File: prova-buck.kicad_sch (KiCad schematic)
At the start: 36 parts, among them J1 Screw_Terminal_01x02, J2 Barrel_Jack, J3 USB_B_Micro, J4 Conn_02x03_Counter_Clockwise, J5 Conn_02x03_Counter_Clockwise, Q1 AO3401A, SW1 SW_SPDT, SW2 SW_SPDT, SW3 SW_SPDT, U1 MPQ9842GL, U2 LDL1117S33R

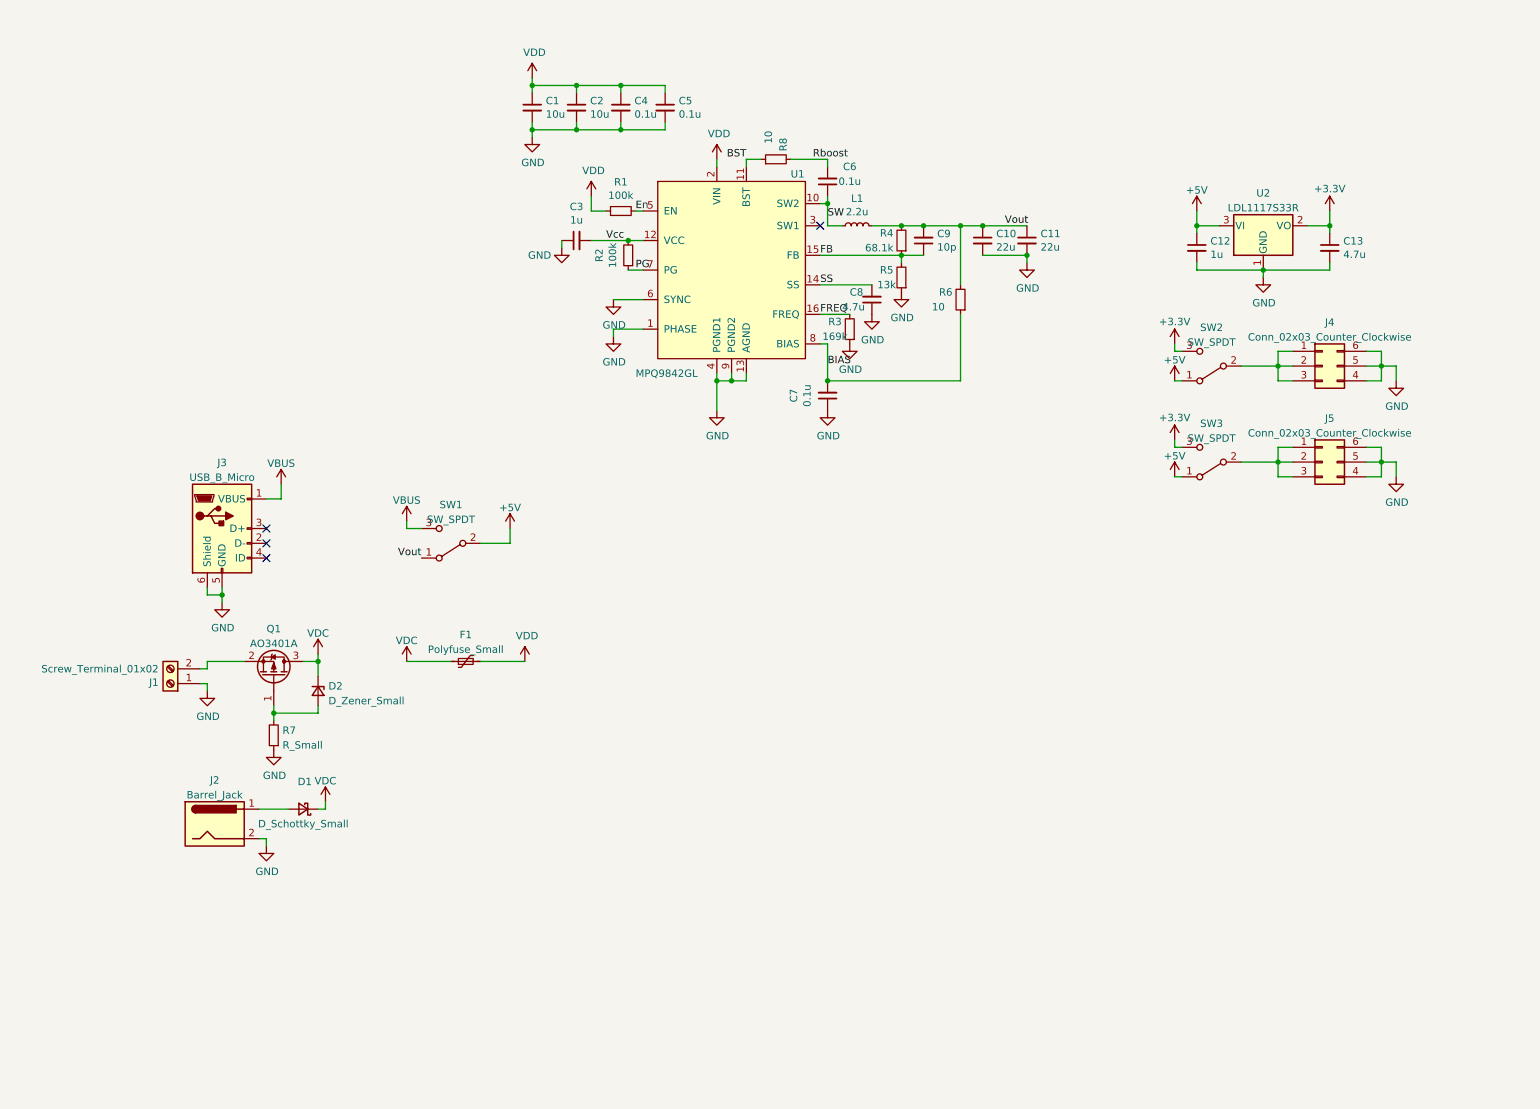
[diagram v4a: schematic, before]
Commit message: "added JLCPB and Mouser components"
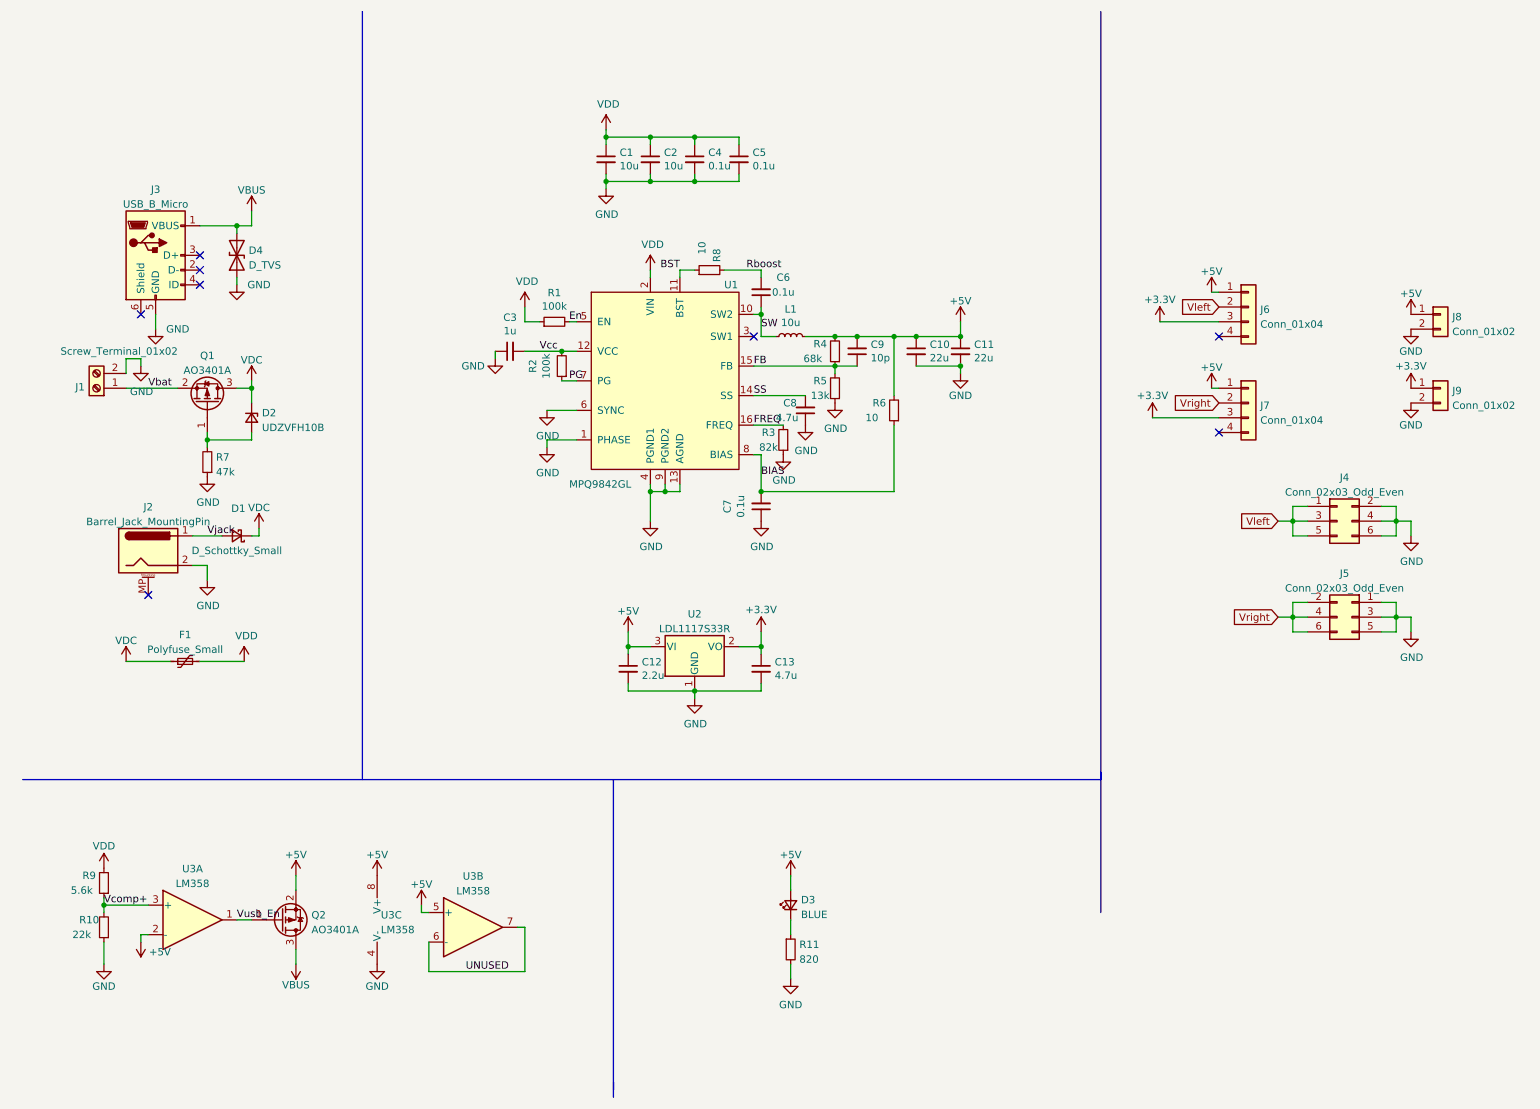
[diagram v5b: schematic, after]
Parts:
- removed J2: Barrel_Jack, Connector_BarrelJack:BarrelJack_Horizontal, symbol Connector:Barrel_Jack
- removed J4: Conn_02x03_Counter_Clockwise, Connector_PinHeader_2.54mm:PinHeader_2x03_P2.54mm_Vertical, symbol Connector_Generic:Conn_02x03_Counter_Clockwise
- removed J5: Conn_02x03_Counter_Clockwise, Connector_PinSocket_2.54mm:PinSocket_2x03_P2.54mm_Vertical, symbol Connector_Generic:Conn_02x03_Counter_Clockwise
- removed SW1: SW_SPDT, Button_Switch_SMD:SW_SPDT_PCM12, symbol Switch:SW_SPDT
- removed SW2, SW3: SW_SPDT, Connector_PinHeader_2.54mm:PinHeader_1x03_P2.54mm_Vertical, symbol Switch:SW_SPDT
- added D3: BLUE, LED_SMD:LED_0603_1608Metric, symbol Device:LED_Small
- added D4: D_TVS, Diode_SMD:D_SOD-323_HandSoldering, symbol Device:D_TVS
- added J2: Barrel_Jack_MountingPin, Connector_BarrelJack:BarrelJack_Horizontal, symbol Connector:Barrel_Jack_MountingPin
- added J4, J5: Conn_02x03_Odd_Even, Connector_PinHeader_2.54mm:PinHeader_2x03_P2.54mm_Vertical, symbol Connector_Generic:Conn_02x03_Odd_Even
- added J6, J7: Conn_01x04, Connector_PinHeader_2.54mm:PinHeader_1x04_P2.54mm_Vertical, symbol Connector_Generic:Conn_01x04
- added J8, J9: Conn_01x02, buck_foot_lib:Solder_wire_PAD, symbol Connector_Generic:Conn_01x02
- added Q2: AO3401A, Package_TO_SOT_SMD:SOT-23, symbol Transistor_FET:AO3401A
- added R10: 22k, Resistor_SMD:R_0603_1608Metric, symbol Device:R_Small
- added R11: 820, Resistor_SMD:R_0603_1608Metric, symbol Device:R_Small
- added R9: 5.6k, Resistor_SMD:R_0603_1608Metric, symbol Device:R_Small
- added U3: LM358, Package_SO:SOIC-8_3.9x4.9mm_P1.27mm, symbol Amplifier_Operational:LM358
- C1, C2: LCSC Part # (none) -> C13585
- C10, C11: footprint Capacitor_SMD:C_0805_2012Metric -> Capacitor_SMD:C_1206_3216Metric; LCSC Part # (none) -> C12891
- C12: value 1u -> 2.2u; footprint Capacitor_SMD:C_0805_2012Metric -> Capacitor_SMD:C_0603_1608Metric; LCSC Part # (none) -> C23630
- C13: LCSC Part # (none) -> C1779
- C3: LCSC Part # (none) -> C15849
- C4, C5, C7: LCSC Part # (none) -> C14663
- C6: LCSC Part # (none) -> C307331
- C8: LCSC Part # (none) -> C19666
- C9: LCSC Part # (none) -> C1634
- D1: footprint Diode_SMD:D_SOD-123 -> Diode_SMD:D_SMA; LCSC Part # (none) -> C8678
- D2: value D_Zener_Small -> UDZVFH10B; footprint Diode_SMD:D_SOD-123 -> Diode_SMD:D_SOD-323_HandSoldering
- F1: footprint Fuse:Fuse_1812_4532Metric -> Fuse:Fuse_2016_HandSolder
- L1: value 2.2u -> 10u; LCSC Part # (none) -> C408412
- Q1: LCSC Part # (none) -> C15127
- R1, R2: LCSC Part # (none) -> C25803
- R3: value 169k -> 82k; LCSC Part # (none) -> C23254
- R4: value 68.1k -> 68k; LCSC Part # (none) -> C23231
- R5: LCSC Part # (none) -> C22797
- R6, R8: LCSC Part # (none) -> C22859
- R7: value R_Small -> 47k; LCSC Part # (none) -> C25819
- U1: footprint buck_foot_lib:MPQ9842GL-Z -> buck_foot_lib:QFN16_3mm_x_4mm
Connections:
- net Vout is gone; now on net +5V: C10.1, C11.1, C9.2, L1.2, R4.2, R6.2
- net +3V3: now also J6.3 (Pin_3), J7.3 (Pin_3), J9.1 (Pin_1)
- net +5V: now also D3.2 (A), J6.1 (Pin_1), J7.1 (Pin_1), J8.1 (Pin_1), Q2.2 (S), U3.2 (-), U3.5 (+), U3.8 (V+)
- net GND: now also J1.2 (Pin_2), D4.1 (A1), J2.2, J4.2 (Pin_2), J4.4 (Pin_4), J4.6 (Pin_6), J5.1 (Pin_1), J5.3 (Pin_3), J5.5 (Pin_5), J8.2 (Pin_2), J9.2 (Pin_2), R10.1, R11.2, U3.4 (V-); no longer J1.1 (Pin_1), J3.6 (Shield)
- net VBUS: now also D4.2 (A2), Q2.3 (D)
- net VDD: now also R9.2
- net Vbat: now reaches Q1.2 (S)
- net Vbat: now also J1.1 (Pin_1); no longer J1.2 (Pin_2)
- net Vjack: now reaches D1.2 (A)
- net Vjack: now also J2.1
- new net: D3.1 (K), R11.1
- new net UNUSED: U3.6 (-), U3.7
- new net Vcomp+: R10.2, R9.1, U3.3 (+)
- new net Vleft: J4.1 (Pin_1), J4.3 (Pin_3), J4.5 (Pin_5), J6.2 (Pin_2)
- new net Vright: J5.2 (Pin_2), J5.4 (Pin_4), J5.6 (Pin_6), J7.2 (Pin_2)
- new net Vusb_En: Q2.1 (G), U3.1
- no-connect marks 4 -> 8
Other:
- moved on the sheet: C1, C10, C11, C12, C13, C2, C3, C4, C5, C6, C7, C8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

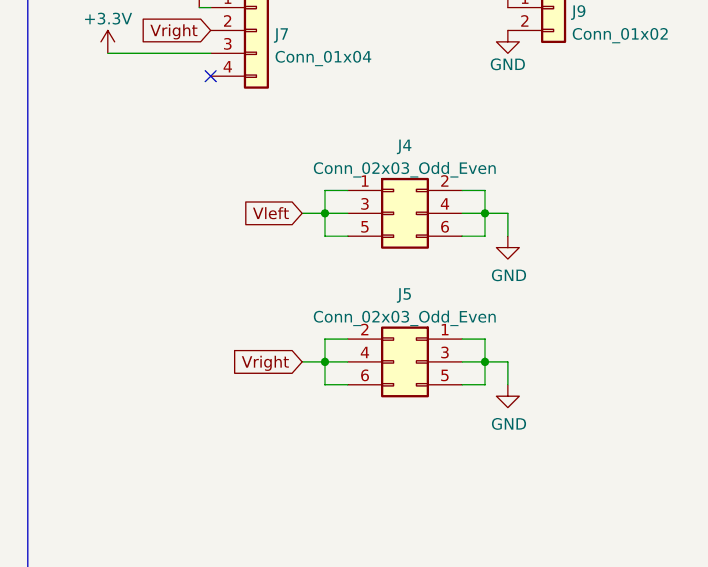
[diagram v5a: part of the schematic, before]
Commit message: Added .gitignore
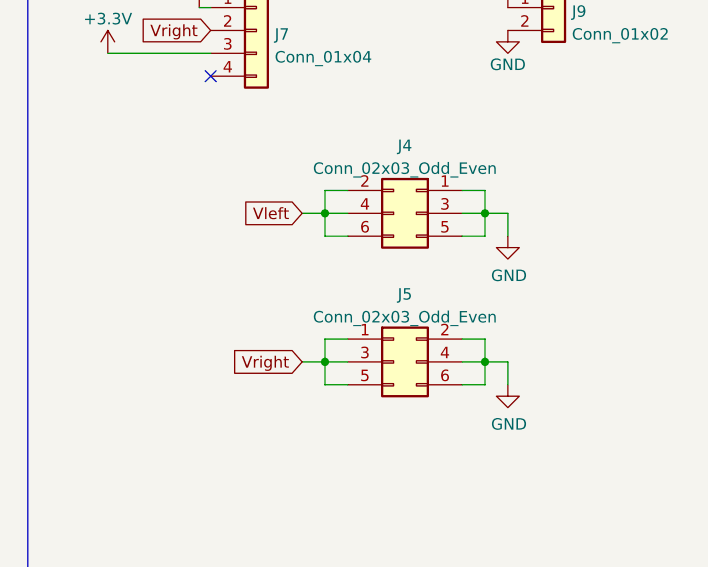
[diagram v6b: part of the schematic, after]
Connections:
- net GND: now also J4.1 (Pin_1), J4.3 (Pin_3), J4.5 (Pin_5), J5.2 (Pin_2), J5.4 (Pin_4), J5.6 (Pin_6); no longer J4.2 (Pin_2), J4.4 (Pin_4), J4.6 (Pin_6), J5.1 (Pin_1), J5.3 (Pin_3), J5.5 (Pin_5)
- net Vleft: now also J4.2 (Pin_2), J4.4 (Pin_4), J4.6 (Pin_6); no longer J4.1 (Pin_1), J4.3 (Pin_3), J4.5 (Pin_5)
- net Vright: now also J5.1 (Pin_1), J5.3 (Pin_3), J5.5 (Pin_5); no longer J5.2 (Pin_2), J5.4 (Pin_4), J5.6 (Pin_6)
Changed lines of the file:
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@@
     (pin "1")
   )
-  (symbol (lib_id "Connector_Generic:Conn_02x03_Odd_Even") (at 241.3 115.57 0) (mirror y) (unit 1)
+  (symbol (lib_id "Connector_Generic:Conn_02x03_Odd_Even") (at 238.76 115.57 0) (unit 1)
     (in_bom yes) (on_board yes) (fields_autoplaced)
     (property "Reference" "J5" (id 0) (at 240.03 108.0602 0))
     (property "Value" "Conn_02x03_Odd_Even" (id 1) (at 240.03 110.5971 0))
-    (property "Footprint" "Connector_PinHeader_2.54mm:PinHeader_2x03_P2.54mm_Vertical" (id 2) (at 241.3 115.57 0)
+    (property "Footprint" "Connector_PinHeader_2.54mm:PinHeader_2x03_P2.54mm_Vertical" (id 2) (at 238.76 115.57 0)
       (effects (font (size 1.27 1.27)) hide)
     )
-    (property "Datasheet" "~" (id 3) (at 241.3 115.57 0)
+    (property "Datasheet" "~" (id 3) (at 238.76 115.57 0)
       (effects (font (size 1.27 1.27)) hide)
     )
@@
     (pin "2")
   )
-  (symbol (lib_id "Connector_Generic:Conn_02x03_Odd_Even") (at 238.76 99.06 0) (unit 1)
+  (symbol (lib_id "Connector_Generic:Conn_02x03_Odd_Even") (at 241.3 99.06 0) (mirror y) (unit 1)
     (in_bom yes) (on_board yes) (fields_autoplaced)
     (property "Reference" "J4" (id 0) (at 240.03 91.5502 0))
     (property "Value" "Conn_02x03_Odd_Even" (id 1) (at 240.03 94.0871 0))
-    (property "Footprint" "Connector_PinHeader_2.54mm:PinHeader_2x03_P2.54mm_Vertical" (id 2) (at 238.76 99.06 0)
+    (property "Footprint" "Connector_PinHeader_2.54mm:PinHeader_2x03_P2.54mm_Vertical" (id 2) (at 241.3 99.06 0)
       (effects (font (size 1.27 1.27)) hide)
     )
-    (property "Datasheet" "~" (id 3) (at 238.76 99.06 0)
+    (property "Datasheet" "~" (id 3) (at 241.3 99.06 0)
       (effects (font (size 1.27 1.27)) hide)
     )

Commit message: "Generated gerbers"
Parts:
- R8: LCSC Part # C22859 -> C25077
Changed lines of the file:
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@@
       (effects (font (size 1.27 1.27)) hide)
     )
-    (property "LCSC Part #" "C22859" (id 4) (at 130.81 55.88 0)
+    (property "LCSC Part #" "C25077" (id 4) (at 130.81 55.88 0)
       (effects (font (size 1.27 1.27)) hide)
     )
